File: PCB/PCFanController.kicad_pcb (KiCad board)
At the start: 2 copper layers, 65.5 x 30 mm, 40 parts, among them J1 USB_C_Receptacle_USB2.0_16P, M1 Fan_4pin, Q1 BSS138, SW1 SW_Push, SW2 SW_Push, SW3 SW_Push, U1 ATtiny404-SS, U2 74HC595, U3 74HC595, U4 OSL40562-LR, U5 AP63203WU, U6 CH221K

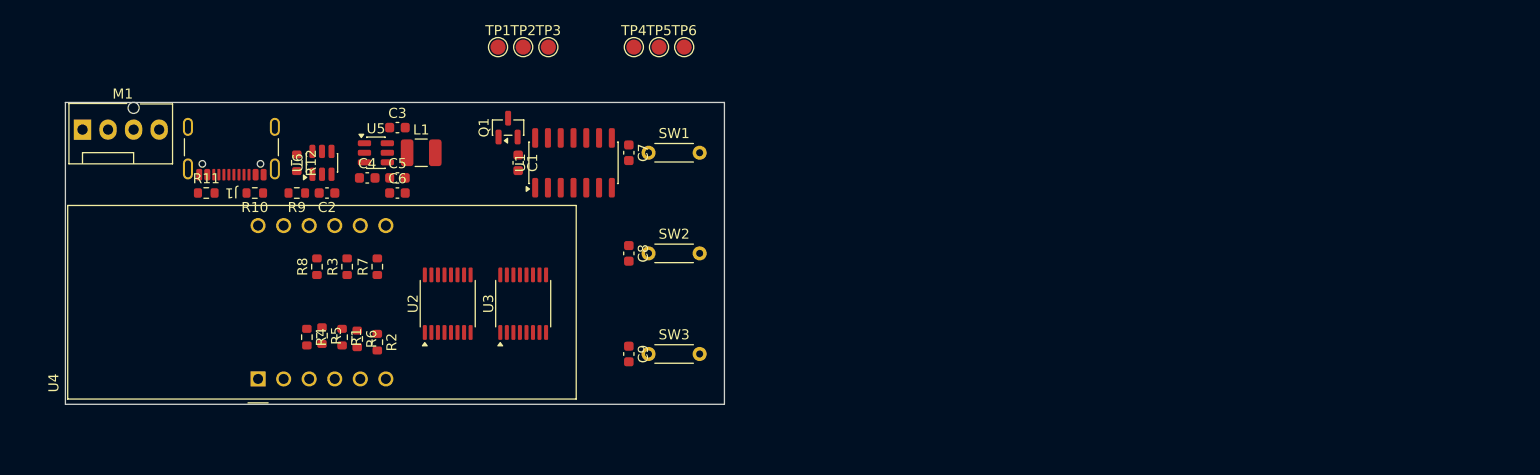
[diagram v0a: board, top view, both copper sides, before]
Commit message: ピンアサイン変更、PCB
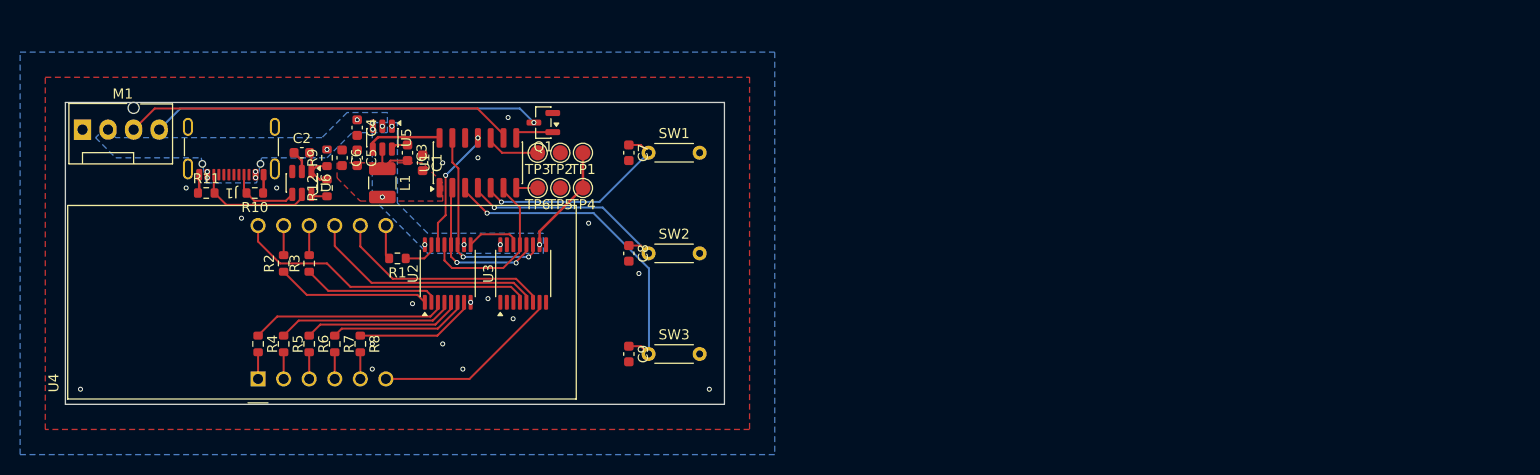
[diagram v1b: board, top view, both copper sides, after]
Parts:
- moved TP6 20.2 mm to (121.4, 88.5), turned to 180 degrees
- moved TP5 17.1 mm to (123.7, 88.5), turned to 180 degrees
- moved TP4 14.9 mm to (125.9, 88.5), turned to 180 degrees
- moved TP1 13.5 mm to (125.9, 85.0), turned to 180 degrees
- moved R2 12.2 mm to (96.2, 96.0), turned to 90 degrees
- moved TP2 11.1 mm to (123.7, 85.0), turned to 180 degrees
- moved TP3 10.6 mm to (121.4, 85.0), turned to 180 degrees
- moved R1 9.56 mm to (107.5, 95.5), turned to 180 degrees
- moved C1 9.50 mm to (110.0, 86.0)
- moved U1 9.50 mm to (115.5, 86.0)
- moved R8 8.80 mm to (103.8, 104.0), turned to -90 degrees
- moved R7 8.76 mm to (101.3, 104.0), turned to -90 degrees
- moved C6 6.52 mm to (102.0, 85.5), turned to -90 degrees
- moved C4 5.10 mm to (103.5, 82.5), turned to -90 degrees
- moved R4 4.90 mm to (93.7, 104.0)
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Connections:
- net /Ctrl-B renamed /Button-Plus
- C7 pad 1: /Ctrl-A -> /Button-Disp
- C9 pad 1: /Ctrl-Push -> /Button-Minus
- R1 pad 2: /7seg-P -> /7seg-B
- R2 pad 2: /7seg-G -> /7seg-A
- R6 pad 2: /7seg-C -> /7seg-P
- R7 pad 2: /7seg-B -> /7seg-C
- R8 pad 2: /7seg-A -> /7seg-G
- SW1 pad 1: /Ctrl-A -> /Button-Disp
- SW3 pad 1: /Ctrl-Push -> /Button-Minus
- U1 pad 3: /Ctrl-A -> /Button-Minus
- U1 pad 5: /Ctrl-Push -> /Button-Disp
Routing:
- net /Tach: track 0.00 -> 39.0 mm
- net Net-(M1-PWM): track 0.00 -> 38.7 mm, vias 0 -> 1
- net /Button-Minus: track 0.00 -> 32.6 mm, vias 0 -> 1
- net /7seg-3: track 0.00 -> 30.5 mm
- net /7seg-2: track 0.00 -> 23.8 mm
- net /Button-Plus: track 0.00 -> 22.1 mm, vias 0 -> 1
- net /7seg-1: track 0.00 -> 21.3 mm
- net /Button-Disp: track 0.00 -> 21.1 mm, vias 0 -> 1
- net /7seg-Clock: track 0.00 -> 20.2 mm, vias 0 -> 2
- net Net-(U2-QD): track 0.00 -> 19.6 mm
- net /7seg-0: track 0.00 -> 18.8 mm
- net Net-(U2-QE): track 0.00 -> 17.7 mm
- net /7seg-En: track 0.00 -> 17.1 mm
- net /7seg-Ratch: track 0.00 -> 15.9 mm, vias 0 -> 2
- net Net-(U2-QF): track 0.00 -> 15.9 mm
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- added copper zone on B.Cu, net +3V3
- added copper zone on F.Cu, net +3V3
- added copper zone on B.Cu, net GND
- added copper zone on F.Cu, net GND
- added copper zone on B.Cu, net VBUS

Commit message: テストポイントをスルーホールに変更
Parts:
- removed TP1, TP2, TP3, TP4, TP5, TP6: TestPoint, TestPoint:TestPoint_Pad_D1.5mm
- added J1: Conn_01x03_Socket, Connector_PinSocket_2.54mm:PinSocket_1x03_P2.54mm_Vertical, F.Cu at (127.0, 85.0)
- added J2: Conn_01x03_Socket, Connector_PinSocket_2.54mm:PinSocket_1x03_P2.54mm_Vertical, F.Cu at (127.0, 88.0)
- renumbered C7 to C2, C2 to C3, C3 to C4, C4 to C5, C8 to C6, C5 to C7, C6 to C8, J1 to J3
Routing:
- net /TX: track 2.14 -> 2.87 mm
- net /UPDI: track 5.48 -> 6.00 mm
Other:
- board text added: "G"
- board text added: "UG3 TG3"

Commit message: 抵抗値修正
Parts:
- R1, R2, R3, R4, R5, R6, R7, R8: value 47 -> 330
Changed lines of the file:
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@@
 			)
 		)
-		(property "Value" "47"
+		(property "Value" "330"
 			(at 0 1.43 90)
 			(layer "F.Fab")
@@
 			)
 		)
-		(property "Value" "47"
+		(property "Value" "330"
 			(at 0 1.43 90)
 			(layer "F.Fab")
@@
 			)
 		)
-		(property "Value" "47"
+		(property "Value" "330"
 			(at 0 1.43 90)
 			(layer "F.Fab")
@@
 			)
 		)
-		(property "Value" "47"
+		(property "Value" "330"
 			(at 0 1.43 90)
 			(layer "F.Fab")
@@
 			)
 		)
-		(property "Value" "47"
+		(property "Value" "330"
 			(at 0 1.43 90)
 			(layer "F.Fab")
@@
 			)
 		)
-		(property "Value" "47"
+		(property "Value" "330"
 			(at 0 1.43 0)
 			(layer "F.Fab")
@@
 			)
 		)
-		(property "Value" "47"
+		(property "Value" "330"
 			(at 0 1.43 90)
 			(layer "F.Fab")
@@
 			)
 		)
-		(property "Value" "47"
+		(property "Value" "330"
 			(at 0 1.43 90)
 			(layer "F.Fab")
@@
 		)
 	)
+	(gr_circle
+		(center 135 85)
+		(end 138 85)
+		(stroke
+			(width 0.1)
+			(type default)
+		)
+		(fill no)
+		(layer "Dwgs.User")
+	)
+	(gr_circle
+		(center 135 95)
+		(end 138 95)
+		(stroke
+			(width 0.1)
+			(type default)
+		)
+		(fill no)
+		(layer "Dwgs.User")
+	)
+	(gr_circle
+		(center 135 105)
+		(end 138 105)
+		(stroke
+			(width 0.1)
+			(type default)
+		)
+		(fill no)
+		(layer "Dwgs.User")
+	)
 	(gr_rect

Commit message: ベタはがした、MOSFET貼った
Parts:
- added Q2: MTN2306AN3, Package_TO_SOT_SMD:SOT-23, F.Cu at (77.5, 88.3)
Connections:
- M1 pad 1: GND -> /Fan-Gnd
- U3 pad 1: unconnected-(U3-QB-Pad1) -> /Fan-Gate
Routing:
- net /Fan-Gate: track 0.00 -> 47.1 mm
- net GND: track 13.4 -> 56.1 mm, vias 18 -> 7
- net /Fan-Gnd: track 0.00 -> 5.73 mm
- net +3V3: track 12.0 -> 11.9 mm, vias 6 -> 7
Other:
- board text added: "+"
- board text added: "-"
- board text added: "DISP"

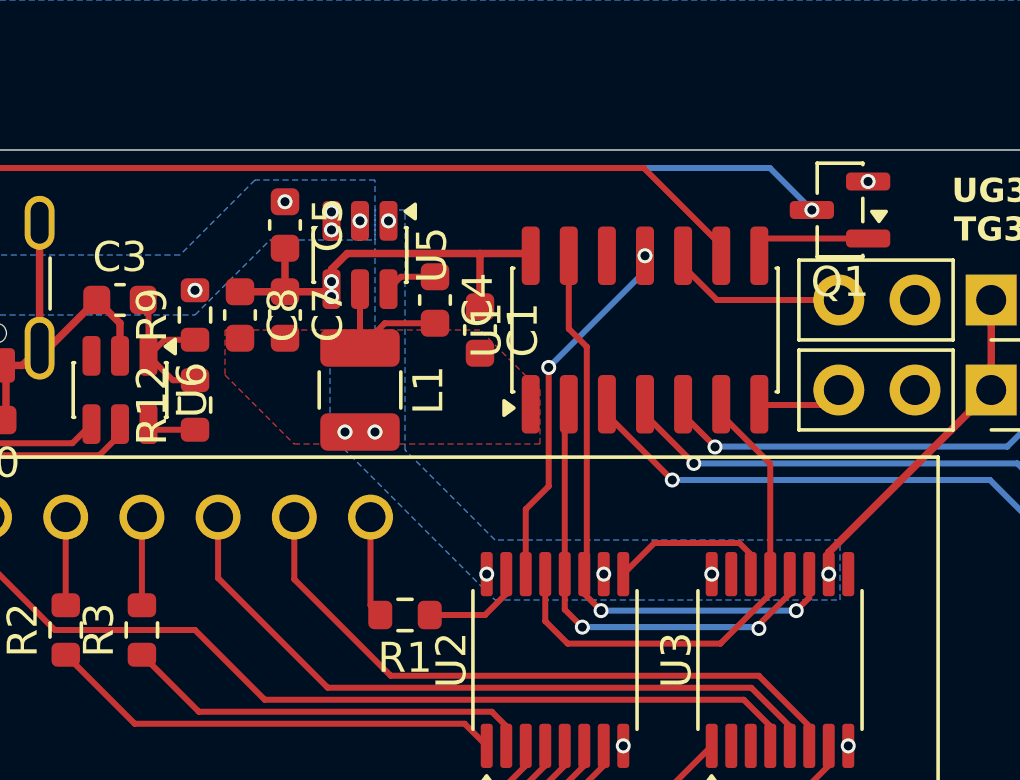
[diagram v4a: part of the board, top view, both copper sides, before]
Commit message: 配線修正
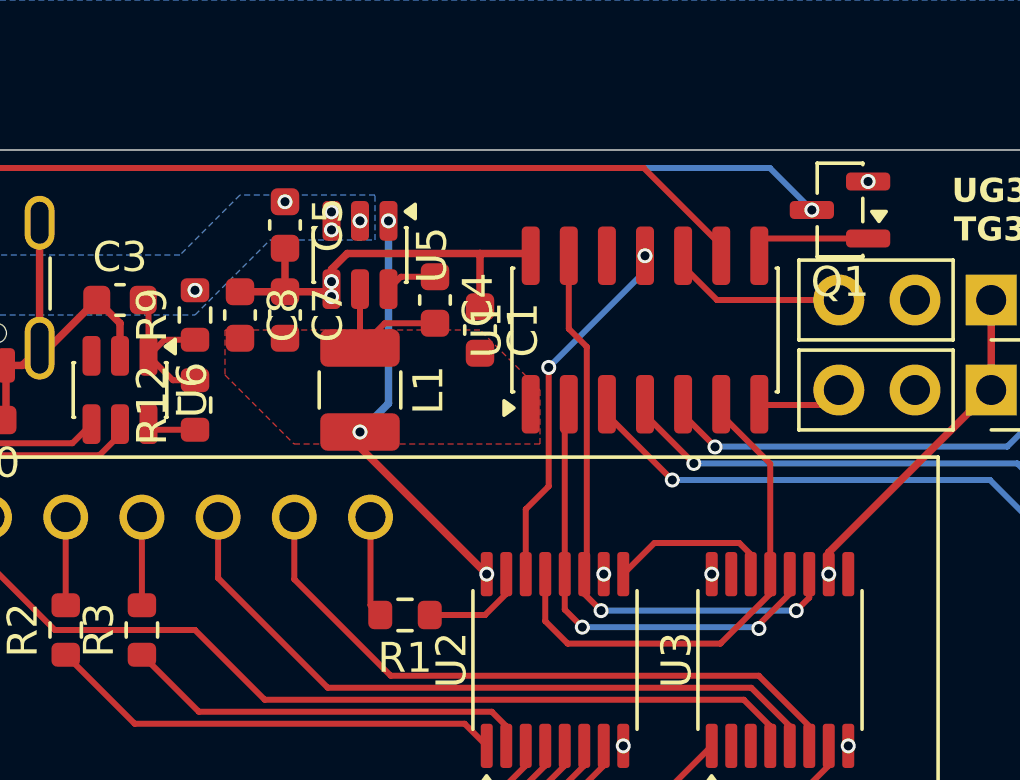
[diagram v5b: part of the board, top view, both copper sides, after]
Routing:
- net +3V3: track 11.9 -> 25.3 mm, vias 7 -> 6
- removed copper zone on B.Cu, net +3V3
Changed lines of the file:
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@@
+	)
+	(segment
+		(start 106 89.9125)
+		(end 106 89.4)
+		(width 0.25)
+		(layer "F.Cu")
+		(net "+3V3")
 	)
 	(segment
@@
 	)
 	(segment
-		(start 110.225 94.1375)
-		(end 110.225 93.625)
-		(width 0.25)
-		(layer "F.Cu")
-		(net "+3V3")
-	)
-	(segment
 		(start 127.04 85)
 		(end 127.04 88)
@@
 		(net "+3V3")
 	)
-	(via
-		(at 105.5 89.4)
-		(size 0.5)
-		(drill 0.3)
-		(layers "F.Cu" "B.Cu")
+	(segment
+		(start 110.225 94.1375)
+		(end 106 89.9125)
+		(width 0.25)
+		(layer "F.Cu")
 		(net "+3V3")
 	)
@@
 	)
 	(via
-		(at 106.5 89.4)
+		(at 106 89.4)
 		(size 0.5)
 		(drill 0.3)
@@
 		(drill 0.3)
 		(layers "F.Cu" "B.Cu")
+		(net "+3V3")
+	)
+	(segment
+		(start 106.95 88.45)
+		(end 106.95 82.3625)
+		(width 0.25)
+		(layer "B.Cu")
+		(net "+3V3")
+	)
+	(segment
+		(start 106 89.4)
+		(end 106.95 88.45)
+		(width 0.25)
+		(layer "B.Cu")
 		(net "+3V3")
 	)
@@
 	)
 	(segment
+		(start 118.04 83.179448)
+		(end 115.460552 80.6)
+		(width 0.2)
+		(layer "F.Cu")
+		(net "/Tach")
+	)
+	(segment
+		(start 115.460552 80.6)
+		(end 83.38 80.6)
+		(width 0.2)
+		(layer "F.Cu")
+		(net "/Tach")
+	)
+	(segment
+		(start 118.04 83.525)
+		(end 118.04 83.179448)
+		(width 0.2)
+		(layer "F.Cu")
+		(net "/Tach")
+	)
+	(segment
 		(start 83.38 80.6)
 		(end 81.28 82.7)
-		(width 0.2)
-		(layer "F.Cu")
-		(net "/Tach")
-	)
-	(segment
-		(start 118.04 83.179448)
-		(end 115.460552 80.6)
-		(width 0.2)
-		(layer "F.Cu")
-		(net "/Tach")
-	)
-	(segment
-		(start 118.04 83.525)
-		(end 118.04 83.179448)
-		(width 0.2)
-		(layer "F.Cu")
-		(net "/Tach")
-	)
-	(segment
-		(start 115.460552 80.6)
-		(end 83.38 80.6)
 		(width 0.2)
 		(layer "F.Cu")
@@
 	)
 	(zone
-		(net "+3V3")
-		(layer "B.Cu")
-		(hatch edge 0.5)
-		(priority 3)
-		(connect_pads
-			(clearance 0.5)
-		)
-		(min_thickness 0.25)
-		(fill yes
-			(thermal_gap 0.5)
-			(thermal_bridge_width 0.5)
-			(island_removal_mode 0)
-		)
-		(polygon
-			(pts
-				(xy 107.5 90) (xy 107.5 82) (xy 106.5 82) (xy 106.5 86) (xy 105 86) (xy 105 89.5) (xy 110.5 95)
-				(xy 122 95) (xy 122 94) (xy 122 93) (xy 110.5 93)
-			)
-		)
-	)
-	(zone
 		(net "VBUS")
 		(layer "B.Cu")
@@
 		(polygon
 			(pts
-				(xy 88 85.5) (xy 88.5 88) (xy 93.5 88) (xy 94 85.5) (xy 100.5 85.5) (xy 103 83) (xy 106.5 83) (xy 106.5 81)
-				(xy 102.5 81) (xy 100 83.5) (xy 89.5 83.5) (xy 79.5 83.5) (xy 78.5 82.5) (xy 77.5 83.5) (xy 79.5 85.5)
+				(xy 88 85.5) (xy 88.5 88) (xy 93.5 88) (xy 94 85.5) (xy 100.5 85.5) (xy 103 83) (xy 106.5 83) (xy 106.5 81.5)
+				(xy 102 81.5) (xy 100 83.5) (xy 89.5 83.5) (xy 79.5 83.5) (xy 78.5 82.5) (xy 77.5 83.5) (xy 79.5 85.5)
 			)
 		)
@@
 		(priority 1)
 		(connect_pads
-			(clearance 0.5)
+			(clearance 0.2)
 		)
 		(min_thickness 0.25)
 		(fill yes
-			(thermal_gap 0.5)
+			(thermal_gap 0.2)
 			(thermal_bridge_width 0.5)
 			(island_removal_mode 0)

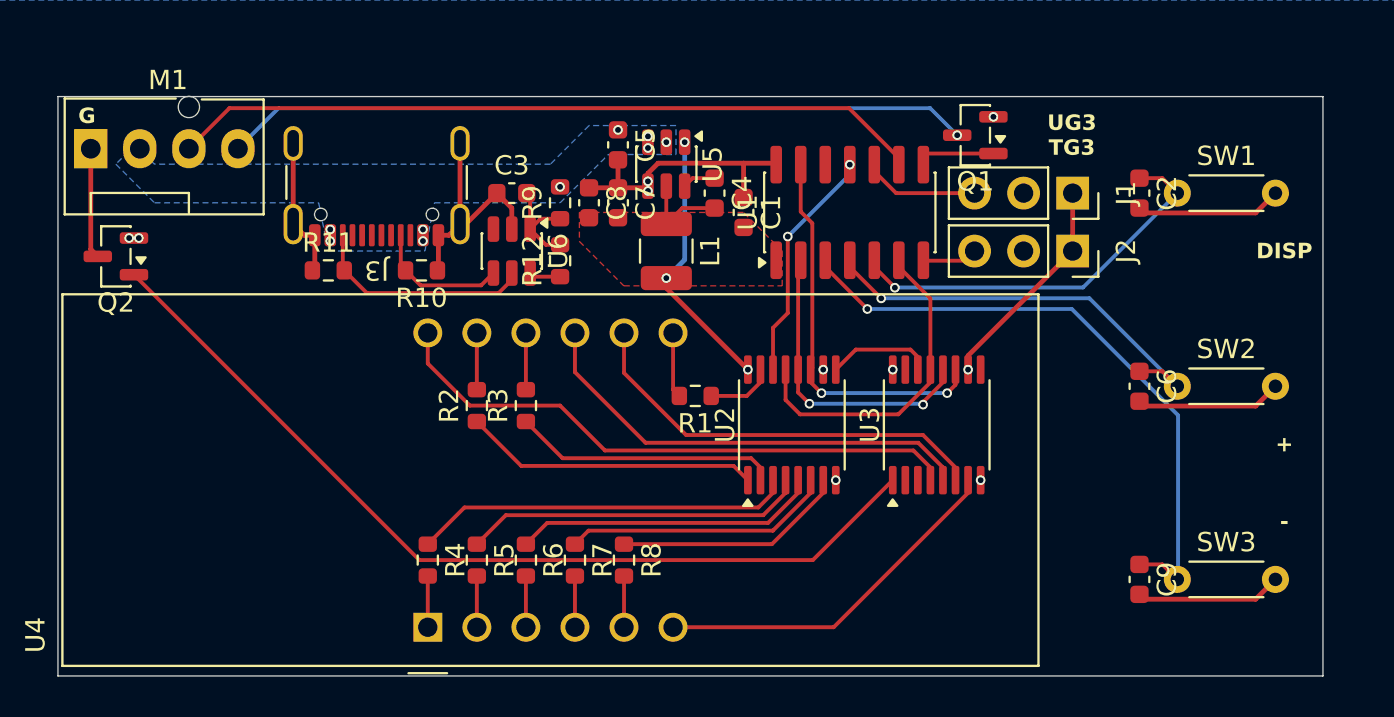
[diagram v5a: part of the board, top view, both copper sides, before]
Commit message: VBus表に、桁選択からENを外し
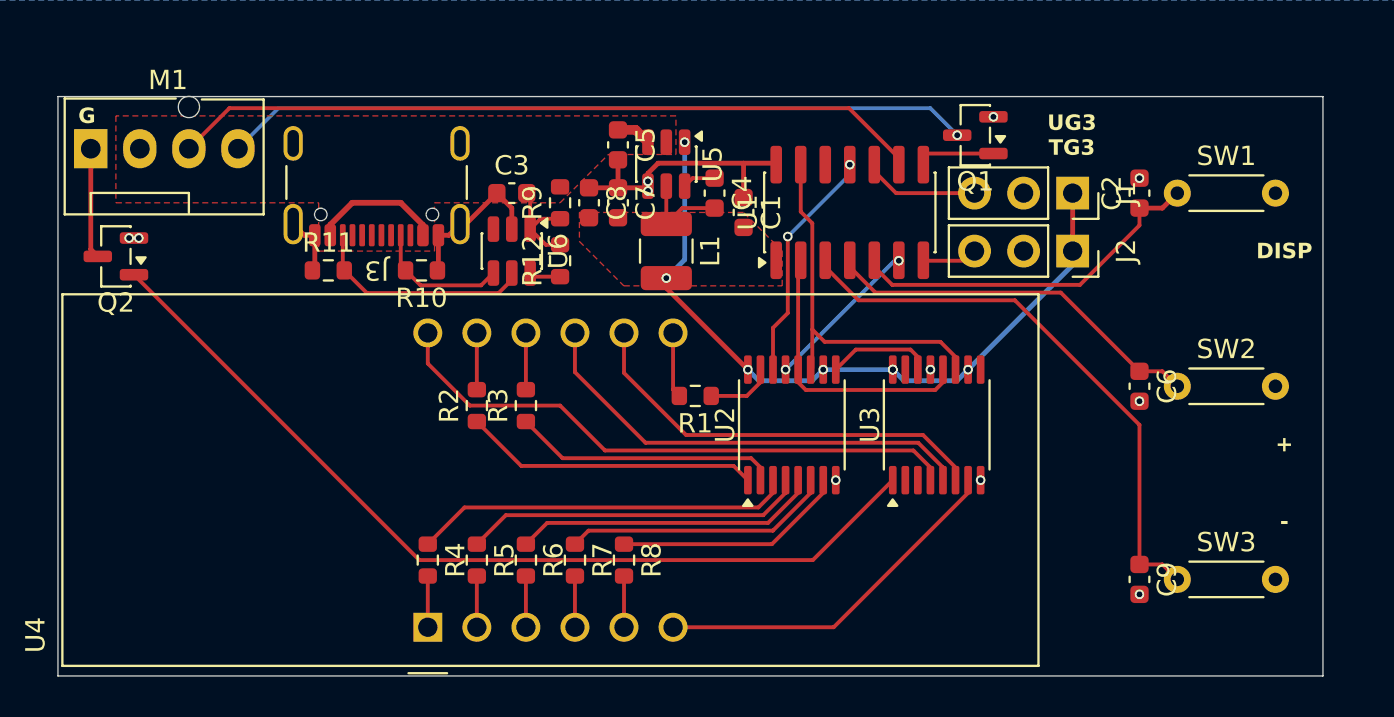
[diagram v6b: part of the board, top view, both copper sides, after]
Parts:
- turned C2 to 90 degrees
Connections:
- U3 pad 13: /7seg-En -> GND
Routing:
- net GND: track 56.1 -> 25.7 mm, vias 7 -> 11
- net +3V3: track 25.3 -> 37.7 mm, vias 6 -> 7
- net VBUS: track 0.05 -> 8.68 mm, vias 9 -> 0
- net /7seg-En: track 17.1 -> 8.61 mm, vias 0 -> 2
- net /Button-Minus: track 32.6 -> 29.6 mm, vias 1 -> 0
- net /Button-Plus: track 22.1 -> 19.9 mm, vias 1 -> 0
- net /Button-Disp: track 21.1 -> 19.3 mm, vias 1 -> 0
- net /7seg-Ratch: track 15.9 -> 14.9 mm, vias 2 -> 0
- net /7seg-Clock: track 20.2 -> 19.6 mm, vias 2 -> 0
- added copper zone on F.Cu, net VBUS
- removed copper zone on B.Cu, net VBUS

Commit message: 配線整理、ベタ塗った
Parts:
- turned C2 to -90 degrees
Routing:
- net GND: track 25.7 -> 4.95 mm, vias 11 -> 17
- net +3V3: track 37.7 -> 44.4 mm, vias 7 -> 9
- net /Button-Plus: track 19.9 -> 22.1 mm
- net /Button-Disp: track 19.3 -> 21.2 mm
- net VBUS: track 8.68 -> 6.87 mm
- net /Button-Minus: track 29.6 -> 31.2 mm
- net /7seg-En: track 8.61 -> 9.80 mm
- net Net-(U2-QH'): track 5.49 -> 6.42 mm
- net /7seg-1: track 21.3 -> 22.1 mm
- net /7seg-Ratch: track 14.9 -> 15.5 mm
- net /7seg-Clock: track 19.6 -> 20.2 mm
- net Net-(U2-QB): track 15.3 -> 15.8 mm

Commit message: びあ
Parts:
- moved R3 5.00 mm to (103.5, 97.5)
- moved R2 4.56 mm to (100.5, 97.5)
- moved R4 3.85 mm to (97.5, 104.0)
- moved R5 3.81 mm to (100.0, 104.0)
- moved R6 3.77 mm to (102.5, 104.0)
- moved R7 3.73 mm to (105.0, 104.0)
- moved R8 3.69 mm to (107.5, 104.0)
- moved R1 0.50 mm to (108.0, 95.5)
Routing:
- net Net-(U2-QC): track 13.8 -> 7.90 mm
- net Net-(U2-QB): track 15.8 -> 10.9 mm
- net Net-(U2-QD): track 19.6 -> 15.8 mm
- net Net-(U2-QE): track 17.7 -> 13.9 mm
- net Net-(U2-QF): track 15.9 -> 12.1 mm
- net Net-(U2-QG): track 14.0 -> 10.2 mm
- net Net-(U2-QH): track 12.1 -> 8.38 mm
- net /7seg-F: track 2.94 -> 6.61 mm
- net /7seg-A: track 2.94 -> 6.22 mm
- net /7seg-E: track 2.65 -> 4.95 mm
- net /7seg-D: track 2.65 -> 4.91 mm
- net /7seg-P: track 2.65 -> 4.87 mm
- net /7seg-C: track 2.65 -> 4.83 mm
- net /7seg-G: track 2.65 -> 4.80 mm
- net /7seg-1: track 22.1 -> 20.7 mm
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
